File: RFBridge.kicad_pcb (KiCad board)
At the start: 4 copper layers, 38.1 x 50.8 mm, 97 parts, among them P1 BNC, P2 BNC, P3 BNC, P4 BNC, U1 CC2520, U2 CC2592, U3 CC1120, U4 CC1190, U5 LDB182G4520C-110, U6 0900PC15J0013, U7 EPCOS_B3588, X1 FA-20H32.0000MF20X-K3, X2 FA-20H32.0000MF20X-K3

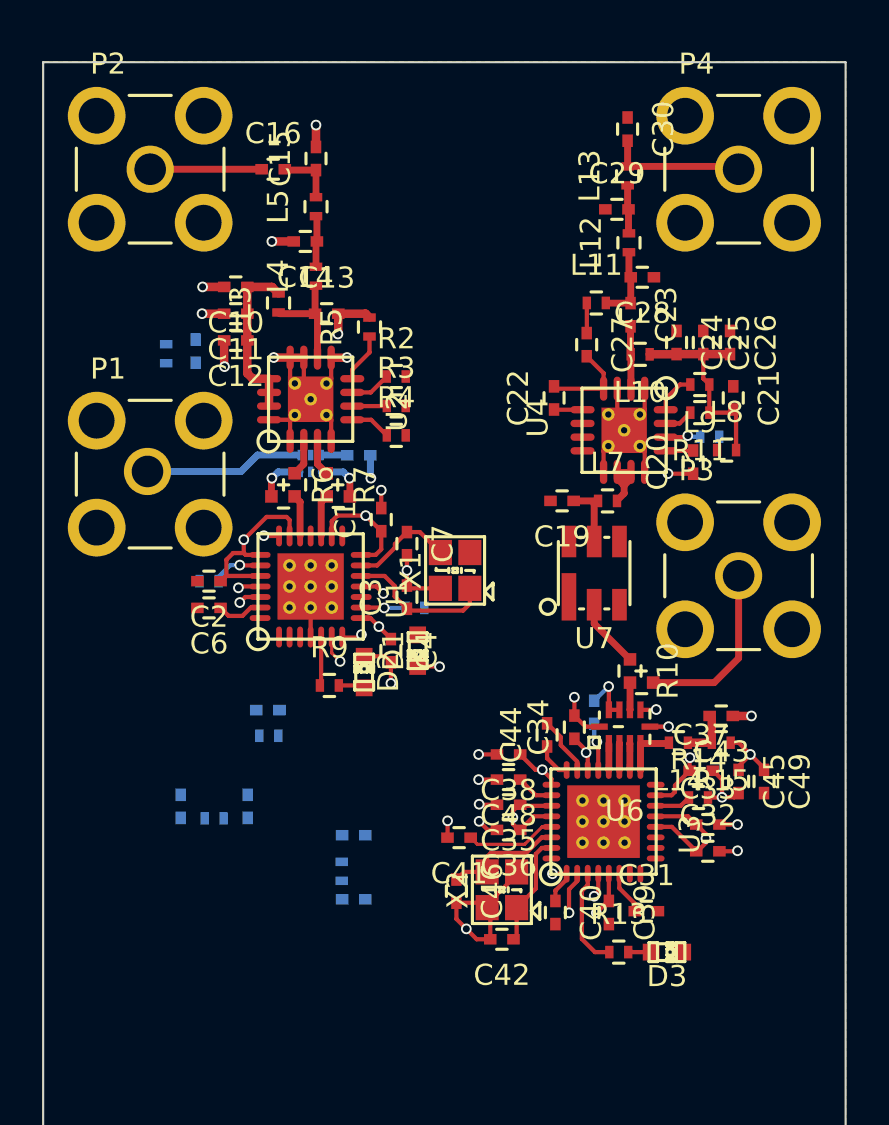
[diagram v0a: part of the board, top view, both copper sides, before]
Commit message: Silk cleanup and some more routing finessing.
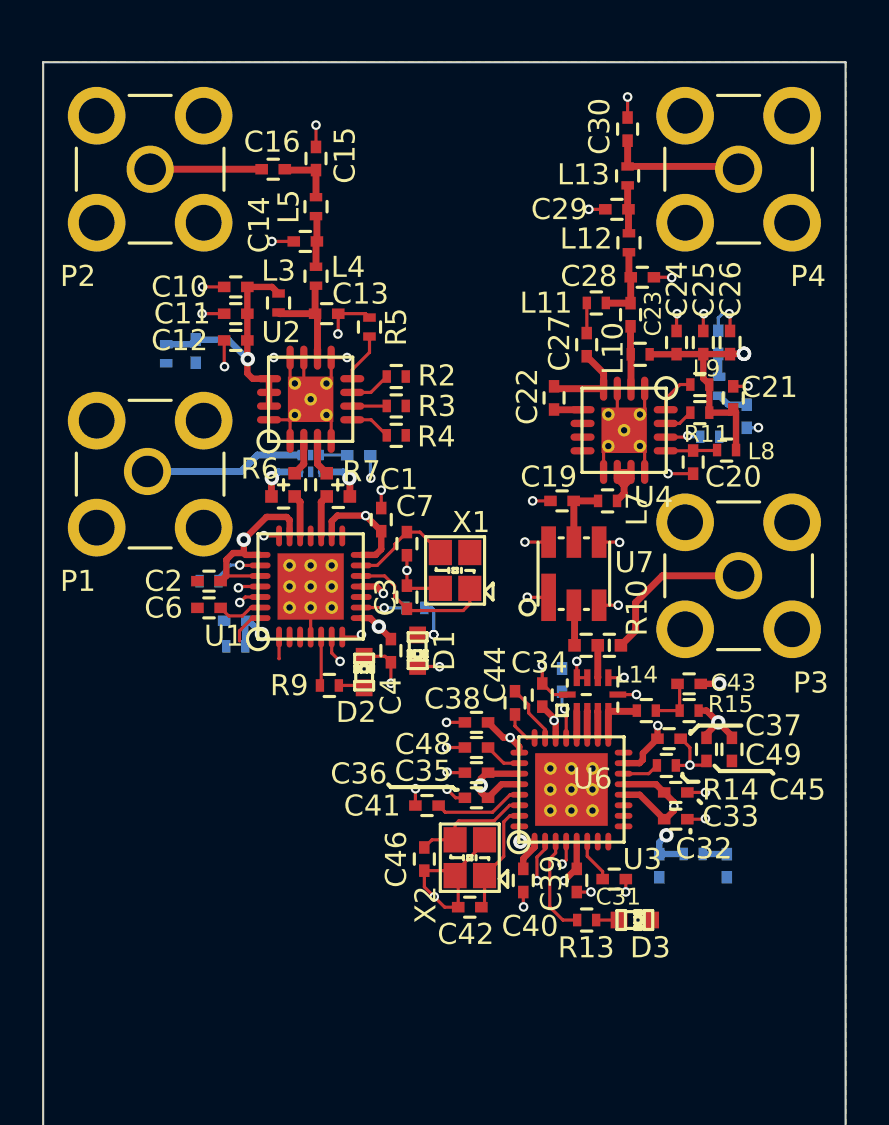
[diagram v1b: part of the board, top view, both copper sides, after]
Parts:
- R10: value 0 -> R3-S; footprint Resistors_SMD:R3_LH_0402 -> Resistors_SMD:R3_S_0402
- moved C17 32.6 mm to (71.5, 54.9)
- moved L6 31.6 mm to (70.2, 53.5), turned to 90 degrees
- moved C18 31.4 mm to (70.2, 51.4), turned to 270 degrees
- moved C50 17.8 mm to (70.6, 76.3), turned to 270 degrees
- moved L15 16.7 mm to (69.0, 75.7), turned to 180 degrees
- moved C51 14.6 mm to (67.4, 76.3), turned to 270 degrees
- moved L1 4.52 mm to (47.2, 65.8), turned to 180 degrees
- moved C5 4.51 mm to (47.2, 64.6), turned to 180 degrees
- moved R10 2.41 mm to (63.9, 65.8), turned to 0 degrees
- moved R13 2.16 mm to (63.9, 78.8)
- moved U3 2.16 mm to (63.2, 72.6)
- moved C31 2.16 mm to (65.2, 76.9)
- moved C32 2.16 mm to (68.1, 74.0)
- moved C33 2.16 mm to (68.1, 72.8)
- moved C34 2.16 mm to (61.8, 68.1)
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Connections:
- net Net-(C13-Pad1) renamed /2G4Radio/ANT1_50
- net Net-(C14-Pad1) renamed /2G4Radio/ANT2_50
- net Net-(C15-Pad1) renamed /2G4Radio/ANT3_50
- net Net-(C16-Pad1) renamed /2G4Radio/ANT4_50
- net Net-(C19-Pad1) renamed /900MRadio/ANT4_50
- net Net-(C22-Pad1) renamed /900MRadio/LNA_IN_50
- net Net-(C22-Pad2) renamed /900MRadio/TR_SW_50
- net Net-(C23-Pad1) renamed /900MRadio/ANT6_50
- net Net-(C23-Pad2) renamed /900MRadio/PA_OUT_50
- net Net-(C29-Pad2) renamed /900MRadio/ANT7_50
- net Net-(C30-Pad2) renamed /900MRadio/ANT8_50
- net Net-(L14-Pad2) renamed /900MRadio/PA
- net Net-(L7-Pad2) renamed /900MRadio/ANT5_50
- net Net-(P1-Pad1) renamed /2G4Radio/ANT5_50
- net Net-(P3-Pad1) renamed /900MRadio/ANT3_50
- net Net-(R10-Pad1) renamed /900MRadio/ANT2_50
- net Net-(R10-Pad2) renamed /900MRadio/ANT1_50
- net Net-(R6-Pad1) renamed /2G4Radio/RF1_N
- net Net-(R6-Pad2) renamed /2G4Radio/RF_N
- net Net-(R6-Pad3) renamed /2G4Radio/RF2_N
- net Net-(R7-Pad1) renamed /2G4Radio/RF1_P
- net Net-(R7-Pad2) renamed /2G4Radio/RF_P
- net Net-(R7-Pad3) renamed /2G4Radio/RF2_P
- net Net-(U3-Pad18) renamed /900MRadio/TRX
- net Net-(U3-Pad19) renamed /900MRadio/LNA_P
- net Net-(U3-Pad20) renamed /900MRadio/LNA_N
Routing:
- net GND: track 69.2 -> 88.1 mm, vias 27 -> 43
- net /900MRadio/VDD_CC1120_ISO: track 26.6 -> 31.6 mm, vias 9 -> 10
- net /2G4Radio/VDD_CC2592_ISO: track 8.15 -> 12.5 mm, vias 0 -> 1
- net /900MRadio/VDD_CC1190_ISO: track 9.90 -> 12.9 mm, vias 0 -> 2
- net /2G4Radio/VDD_CC2520_ISO: track 29.5 -> 32.4 mm, vias 4 -> 5
- net Net-(D1-Pad2): track 0.00 -> 2.43 mm, vias 0 -> 2
- net /2G4Radio/SCLK: track 0.00 -> 1.71 mm
- net /900MRadio/VDD_CC1190: track 0.00 -> 1.48 mm
- net /900MRadio/ANT2_50: track 3.30 -> 1.92 mm
- net /900MRadio/VDD_CC1120: track 0.00 -> 1.15 mm
- net Net-(C20-Pad2): track 1.31 -> 2.45 mm
- net /2G4Radio/MISO: track 0.00 -> 1.03 mm
- net /900MRadio/ANT3_50: track 8.45 -> 7.74 mm
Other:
- net class 50ohm: clearance 0.3302 -> 0.1524; via_dia 0.3556 -> 0.6858; via_drill 0.254 -> 0.3302
- net class Default: via_dia 0.3556 -> 0.4572
- net class RF_Power added: clearance 0.1524, trace_width 0.3048, via_dia 0.6858, via_drill 0.3302
- rule via_min_size: 0.3556 -> 0.4572

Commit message: Compressed design a bit.
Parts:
- added FD1: FIDUCIAL, Fiducials:Fiducial_1mm_Dia_2.54mm_Outer_CopperBottom, F.Cu at (49.0, 40.1)
- added FD2: FIDUCIAL, Fiducials:Fiducial_1mm_Dia_2.54mm_Outer_CopperBottom, F.Cu at (72.1, 80.5)
- added FD3: FIDUCIAL, Fiducials:Fiducial_1mm_Dia_2.54mm_Outer_CopperTop, F.Cu at (49.0, 40.1)
- added FD4: FIDUCIAL, Fiducials:Fiducial_1mm_Dia_2.54mm_Outer_CopperTop, F.Cu at (72.1, 80.8)
- U2: footprint RGV_S-PVQFN-N16 -> SMD_Packages:RGV_S-PVQFN-N16
- moved C47 2.65 mm to (60.2, 68.1), turned to 180 degrees
- moved C40 2.01 mm to (58.9, 77.1)
- moved C45 2.01 mm to (67.6, 70.9)
- moved C50 2.01 mm to (68.6, 76.4)
- moved D3 2.01 mm to (64.2, 79.0)
- moved L14 2.01 mm to (64.7, 69.0)
- moved R14 2.01 mm to (65.7, 71.6)
- moved C31 2.01 mm to (63.2, 77.0)
- moved C34 2.01 mm to (59.8, 68.3)
- moved C35 2.01 mm to (56.7, 72.0)
- moved C36 2.01 mm to (56.7, 73.2)
- moved C38 2.01 mm to (56.7, 69.6)
- moved C39 2.01 mm to (61.4, 77.1)
- moved C41 2.01 mm to (54.3, 73.5)
- moved C42 2.01 mm to (56.3, 78.4)
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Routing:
- net /900MRadio/ANT3_50: track 7.74 -> 8.83 mm
- net /900MRadio/ANT4_50: track 3.12 -> 3.87 mm
- net GND: track 88.1 -> 87.5 mm, vias 43 -> 41
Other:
- board size 38.1 x 50.8 mm -> 36.2 x 44.4 mm

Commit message: Added XMC4500.sch
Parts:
- added U8: XMC4500F100, Housings_QFP:LQFP-100-1EP_14x14mm_Pitch0.5mm, B.Cu at (48.5, 76.2)
- U3: value CC1120 -> CC1200
- moved C19 0.19 mm to (61.0, 58.9)
- moved L7 0.19 mm to (63.4, 58.9)

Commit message: Added capacitors for XMC chip, diagram of power tree, and more connectors.
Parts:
- added C52: 12p, Capacitors_SMD:C_0402, F.Cu at (68.0, 103.1)
- added C53: 12p, Capacitors_SMD:C_0402, F.Cu at (81.9, 100.4)
- added C54: 0.1u, Capacitors_SMD:C_0402, F.Cu at (85.4, 95.0)
- added C55: 0.1u, Capacitors_SMD:C_0402, F.Cu at (69.0, 108.5)
- added C56: 10u, Capacitors_SMD:C_0603, F.Cu at (78.1, 95.2)
- added C57: 10u, Capacitors_SMD:C_0603, F.Cu at (57.6, 103.3)
- added C58: 0.1u, Capacitors_SMD:C_0402, F.Cu at (75.3, 106.2)
- added C59: 0.1u, Capacitors_SMD:C_0402, F.Cu at (65.2, 108.5)
- added C60: 0.1u, Capacitors_SMD:C_0402, F.Cu at (71.5, 103.1)
- added C61: 0.1u, Capacitors_SMD:C_0402, F.Cu at (81.7, 95.0)
- added C62: 0.1u, Capacitors_SMD:C_0402, F.Cu at (57.8, 108.9)
- added C63: 0.1u, Capacitors_SMD:C_0402, F.Cu at (64.5, 103.1)
- added C64: 0.1u, Capacitors_SMD:C_0402, F.Cu at (61.5, 108.7)
- added C65: 0.1u, Capacitors_SMD:C_0402, F.Cu at (78.3, 100.8)
- added L16: BLM18PG600SN1D, Resistors_SMD:R_0603, F.Cu at (62.9, 118.1)
- added P5: USB_B, Connect:USB_Micro-B, F.Cu at (74.8, 119.6)
- added R16: 10k, Resistors_SMD:R_0402, F.Cu at (60.9, 103.2)
- added R17: 33, Resistors_SMD:R_0402, F.Cu at (60.9, 123.8)
- added R18: 33, Resistors_SMD:R_0402, F.Cu at (57.6, 123.8)
- added X3: FA-20H24.0000MF20Z-K3, Crystals_Oscillators_SMD:FA-20H, F.Cu at (66.2, 95.4)
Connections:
- net /2G4Radio/CCA renamed /XMC4500/CC2520_CCA
- net /2G4Radio/CS_L renamed /XMC4500/CC2520_CS
- net /2G4Radio/FIFO renamed /XMC4500/CC2520_FIFO
- net /2G4Radio/FIFOP renamed /XMC4500/CC2520_FIFOP
- net /2G4Radio/HGM renamed /XMC4500/CC2592_HGM
- net /2G4Radio/LNA_EN renamed /XMC4500/CC2592_LNA_EN
- net /2G4Radio/PA_EN renamed /XMC4500/CC2592_PA_EN
- net /2G4Radio/RESET_L renamed /XMC4500/CC2520_RESET
- net /2G4Radio/SFD renamed /XMC4500/CC2520_SFD
- net /2G4Radio/VREG_EN renamed /XMC4500/CC2520_VREG_EN
- net /900MRadio/CS_L renamed /XMC4500/CC1200_CS
- net /900MRadio/GPIO0 renamed /XMC4500/CC1200_GPIO0
- net /900MRadio/GPIO2 renamed /XMC4500/CC1200_GPIO2
- net /900MRadio/GPIO3 renamed /XMC4500/CC1200_GPIO3
- net /900MRadio/HGM renamed /XMC4500/CC1190_HGM
- net /900MRadio/LNA_EN renamed /XMC4500/CC1190_LNA_EN
- net /900MRadio/PA_EN renamed /XMC4500/CC1190_PA_EN
- net /900MRadio/RESET_L renamed /XMC4500/CC1200_RESET
- net /900MRadio/VDD_CC1120 renamed /900MRadio/VDD_CC1200
- net /900MRadio/VDD_CC1120_ISO renamed /900MRadio/VDD_CC1200_ISO
- net Net-(U8-Pad65) renamed /XMC4500/RESET_L
- U1 pad 28: /2G4Radio/SCLK -> /XMC4500/RADIO_SCLK
- U3 pad 7: /900MRadio/MOSI -> /2G4Radio/MOSI
- U3 pad 8: /900MRadio/SCLK -> /XMC4500/RADIO_SCLK
- U3 pad 9: /900MRadio/MISO -> /2G4Radio/MISO
- U8 pad 10: Net-(U8-Pad10) -> +5VUSB
- U8 pad 101: Net-(U8-Pad101) -> GND
- U8 pad 11: Net-(U8-Pad11) -> /XMC4500/VDD_MCU
- U8 pad 12: Net-(U8-Pad12) -> /XMC4500/VDD_MCU
- U8 pad 17: Net-(U8-Pad17) -> /XMC4500/VDD_MCU
- U8 pad 32: Net-(U8-Pad32) -> GND
- U8 pad 33: Net-(U8-Pad33) -> /XMC4500/VDD_MCU
- U8 pad 34: Net-(U8-Pad34) -> GND
- U8 pad 35: Net-(U8-Pad35) -> /XMC4500/VDD_MCU
- U8 pad 42: Net-(U8-Pad42) -> /XMC4500/VDD_MCU
- U8 pad 43: Net-(U8-Pad43) -> /XMC4500/VDD_MCU
- U8 pad 59: Net-(U8-Pad59) -> GND
- U8 pad 60: Net-(U8-Pad60) -> /XMC4500/VDD_MCU
- U8 pad 63: Net-(U8-Pad63) -> GND
- U8 pad 64: Net-(U8-Pad64) -> /XMC4500/VDD_MCU
- U8 pad 8: Net-(U8-Pad8) -> /XMC4500/USB_N
- U8 pad 86: Net-(U8-Pad86) -> /XMC4500/VDD_MCU
- U8 pad 87: Net-(U8-Pad87) -> /XMC4500/VDD_MCU
- U8 pad 9: Net-(U8-Pad9) -> /XMC4500/USB_P
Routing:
- net /XMC4500/RADIO_SCLK: track 0.00 -> 1.71 mm
- net /2G4Radio/SCLK: track 1.71 -> 0.00 mm
- net Net-(U8-Pad56): track 0.00 -> 0.62 mm, vias 0 -> 1
- net /900MRadio/VDD_CC1200_ISO: track 31.6 -> 31.0 mm, vias 10 -> 9
- net Net-(U8-Pad50): vias 0 -> 1
- net GND: vias 41 -> 40
- added copper zone on In2.Cu, net /900MRadio/VDD_CC1120_ISO
- removed copper zone on In2.Cu, net /900MRadio/VDD_CC1200_ISO

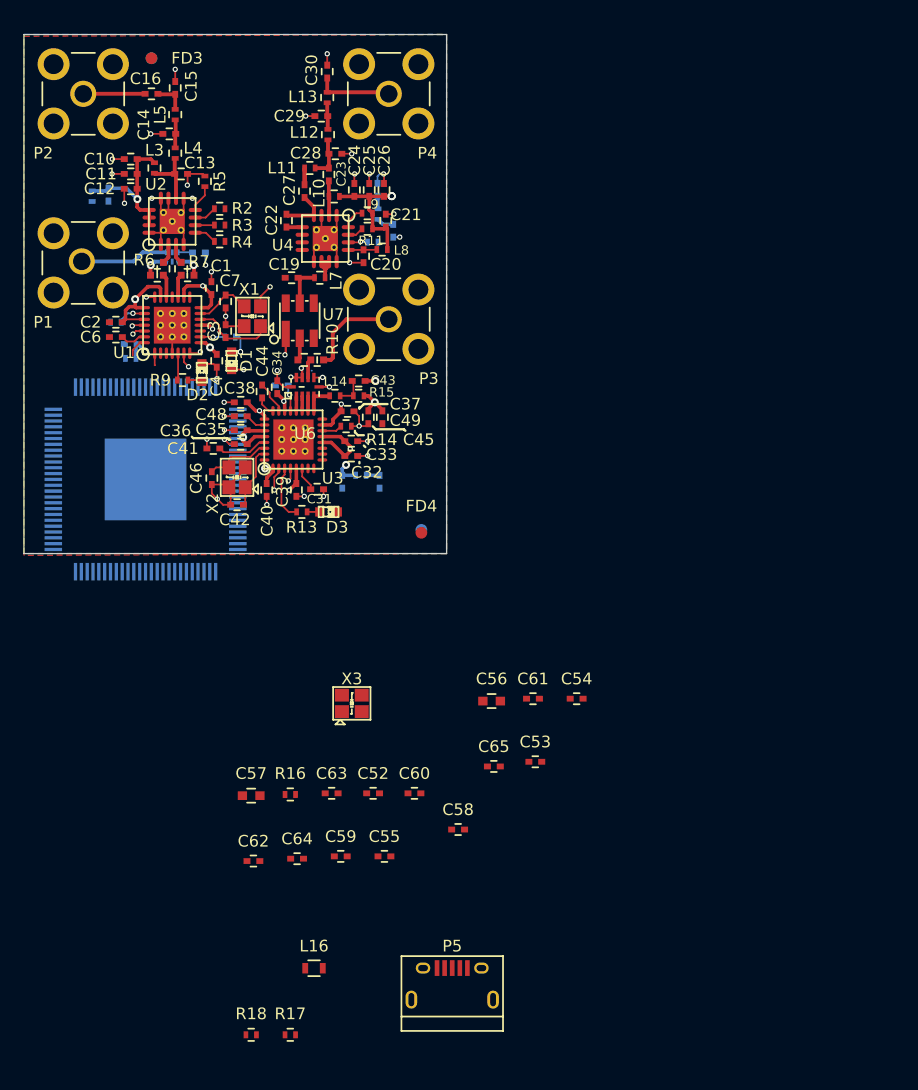
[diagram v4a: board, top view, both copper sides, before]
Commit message: Added 3.3V LDO
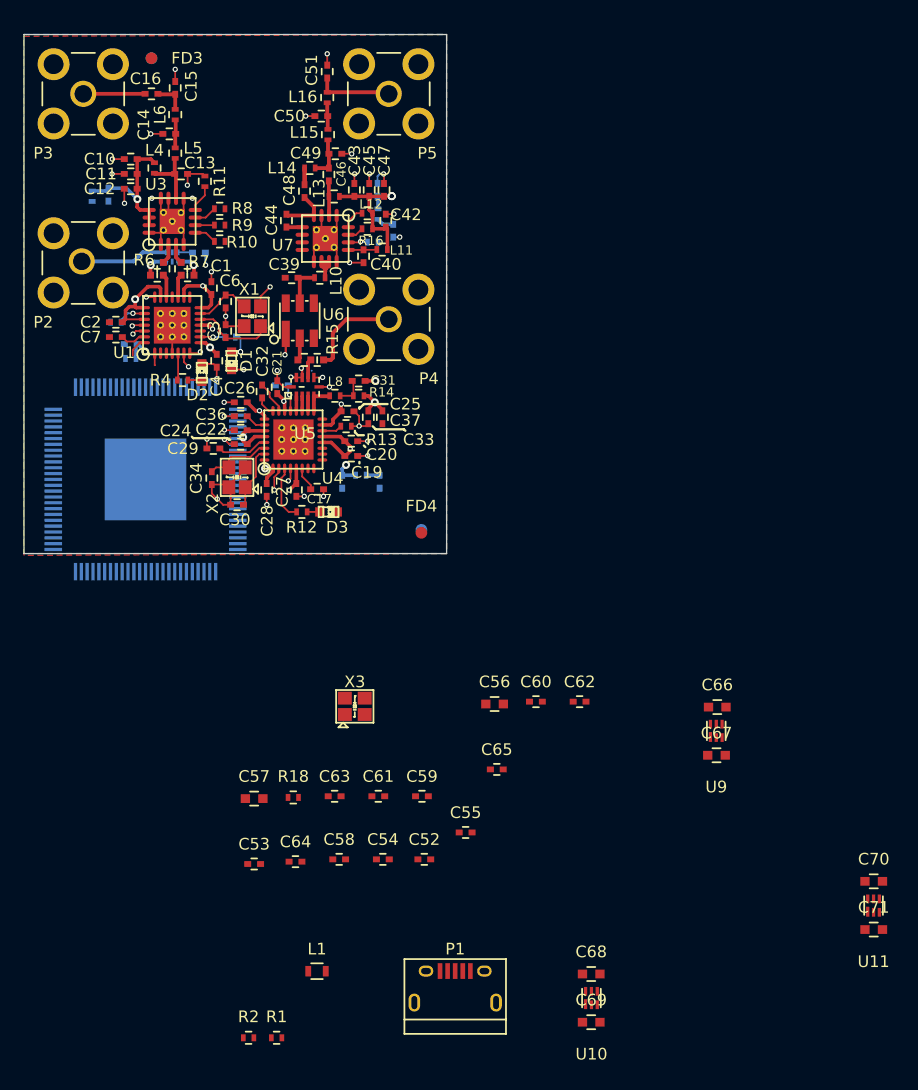
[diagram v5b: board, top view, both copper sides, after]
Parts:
- removed the P5 at (74.8, 119.6)
- added C66: 1u, Capacitors_SMD:C_0603, F.Cu at (97.5, 95.7)
- added C67: 1u, Capacitors_SMD:C_0603, F.Cu at (97.4, 99.8)
- added C68: 1u, Capacitors_SMD:C_0603, F.Cu at (86.7, 118.6)
- added C69: 1u, Capacitors_SMD:C_0603, F.Cu at (86.7, 122.7)
- added C70: 1u, Capacitors_SMD:C_0603, F.Cu at (110.9, 110.6)
- added C71: 1u, Capacitors_SMD:C_0603, F.Cu at (110.9, 114.7)
- added P1: USB_OTG, Connect:USB_Micro-B, F.Cu at (75.0, 119.9)
- added U10: TPS727, SMD_Packages:S-PWSON-N6, F.Cu at (86.7, 120.6)
- added U11: TPS727, SMD_Packages:S-PWSON-N6, F.Cu at (110.9, 112.7)
- added U9: TPS727, SMD_Packages:S-PWSON-N6, F.Cu at (97.4, 97.7)
- moved C62 31.1 mm to (85.7, 95.2)
- moved C53 25.6 mm to (57.8, 109.1)
- moved C54 21.6 mm to (68.8, 108.7)
- moved C61 15.7 mm to (68.4, 103.3)
- moved C60 13.0 mm to (81.9, 95.2)
- moved C58 10.5 mm to (65.1, 108.7)
- moved C59 8.65 mm to (72.2, 103.3)
- moved C55 7.25 mm to (75.9, 106.4)
- moved C52 7.15 mm to (72.4, 108.7)
- moved R1 1.20 mm to (59.7, 124.0)
- moved C65 0.36 mm to (78.6, 101.0)
- moved C57 0.36 mm to (57.8, 103.5)
- moved L1 0.36 mm to (63.2, 118.3)
- moved R18 0.36 mm to (61.2, 103.4)
- moved C56 0.36 mm to (78.4, 95.4)
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- renumbered C31 to C17, C50 to C18, C32 to C19, C33 to C20, C34 to C21, C35 to C22, C51 to C23, C36 to C24, C37 to C25, C38 to C26, C39 to C27, C40 to C28, C41 to C29, C42 to C30, C43 to C31, C44 to C32, C45 to C33, C46 to C34, C47 to C35, C48 to C36, C49 to C37, C17 to C38, C19 to C39, C20 to C40, C18 to C41, C21 to C42, C24 to C43, C22 to C44, C25 to C45, C23 to C46, C26 to C47, C27 to C48, C28 to C49, C29 to C50, C30 to C51, C7 to C6, C6 to C7, L16 to L1, L7 to L10, L8 to L11, L9 to L12, L10 to L13, L11 to L14, L12 to L15, L13 to L16, L1 to L2, L2 to L3, L3 to L4, L4 to L5, L5 to L6, L15 to L7, L14 to L8, L6 to L9, P1 to P2, P2 to P3, P3 to P4, P4 to P5, R17 to R1, R4 to R10, R5 to R11, R13 to R12, R14 to R13, R15 to R14, R10 to R15, R11 to R16, R12 to R17, R16 to R18, R18 to R2, R8 to R3, R9 to R4, R1 to R5, R2 to R8, R3 to R9, U5 to U2, U2 to U3, U3 to U4, U6 to U5, U7 to U6, U4 to U7
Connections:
- C19 pad 1: /900MRadio/VDD_CC1200_ISO -> /900MRadio/VDD_CC1120_ISO
- C20 pad 1: /900MRadio/VDD_CC1200_ISO -> /900MRadio/VDD_CC1120_ISO
- C21 pad 1: /900MRadio/VDD_CC1200_ISO -> /900MRadio/VDD_CC1120_ISO
- C22 pad 1: /900MRadio/VDD_CC1200_ISO -> /900MRadio/VDD_CC1120_ISO
- C23 pad 1: /900MRadio/VDD_CC1200_ISO -> /900MRadio/VDD_CC1120_ISO
- C24 pad 1: /900MRadio/VDD_CC1200_ISO -> /900MRadio/VDD_CC1120_ISO
- C25 pad 1: /900MRadio/VDD_CC1200_ISO -> /900MRadio/VDD_CC1120_ISO
- C26 pad 1: /900MRadio/VDD_CC1200_ISO -> /900MRadio/VDD_CC1120_ISO
- C27 pad 1: /900MRadio/VDD_CC1200_ISO -> /900MRadio/VDD_CC1120_ISO
- C28 pad 1: /900MRadio/VDD_CC1200_ISO -> /900MRadio/VDD_CC1120_ISO
- C31 pad 1: /900MRadio/VDD_CC1200_ISO -> /900MRadio/VDD_CC1120_ISO
- C33 pad 1: /900MRadio/VDD_CC1200_ISO -> /900MRadio/VDD_CC1120_ISO
- C37 pad 1: /900MRadio/VDD_CC1200_ISO -> /900MRadio/VDD_CC1120_ISO
- L7 pad 2: /900MRadio/VDD_CC1200_ISO -> /900MRadio/VDD_CC1120_ISO
- R14 pad 1: /900MRadio/VDD_CC1200_ISO -> /900MRadio/VDD_CC1120_ISO
- U4 pad 1: /900MRadio/VDD_CC1200_ISO -> /900MRadio/VDD_CC1120_ISO
- U4 pad 12: /900MRadio/VDD_CC1200_ISO -> /900MRadio/VDD_CC1120_ISO
- U4 pad 13: /900MRadio/VDD_CC1200_ISO -> /900MRadio/VDD_CC1120_ISO
- U4 pad 15: /900MRadio/VDD_CC1200_ISO -> /900MRadio/VDD_CC1120_ISO
- U4 pad 22: /900MRadio/VDD_CC1200_ISO -> /900MRadio/VDD_CC1120_ISO
- U4 pad 25: /900MRadio/VDD_CC1200_ISO -> /900MRadio/VDD_CC1120_ISO
- U4 pad 27: /900MRadio/VDD_CC1200_ISO -> /900MRadio/VDD_CC1120_ISO
- U4 pad 28: /900MRadio/VDD_CC1200_ISO -> /900MRadio/VDD_CC1120_ISO
- U4 pad 5: /900MRadio/VDD_CC1200_ISO -> /900MRadio/VDD_CC1120_ISO
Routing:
- net /900MRadio/VDD_CC1120_ISO: track 0.00 -> 31.6 mm, vias 0 -> 9
- net /900MRadio/VDD_CC1200_ISO: track 31.0 -> 0.00 mm, vias 9 -> 0
- net Net-(U8-Pad56): track 0.62 -> 0.00 mm
